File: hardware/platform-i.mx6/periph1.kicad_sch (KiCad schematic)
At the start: 18 parts, among them J1 SD-104031, J3 TC2030-IDC, J6 UART5, J7 I2C4, J8 ECSPI4, U1 IMX6UL_BGA289, U3 TJA1051T, U5 RFM69HCW

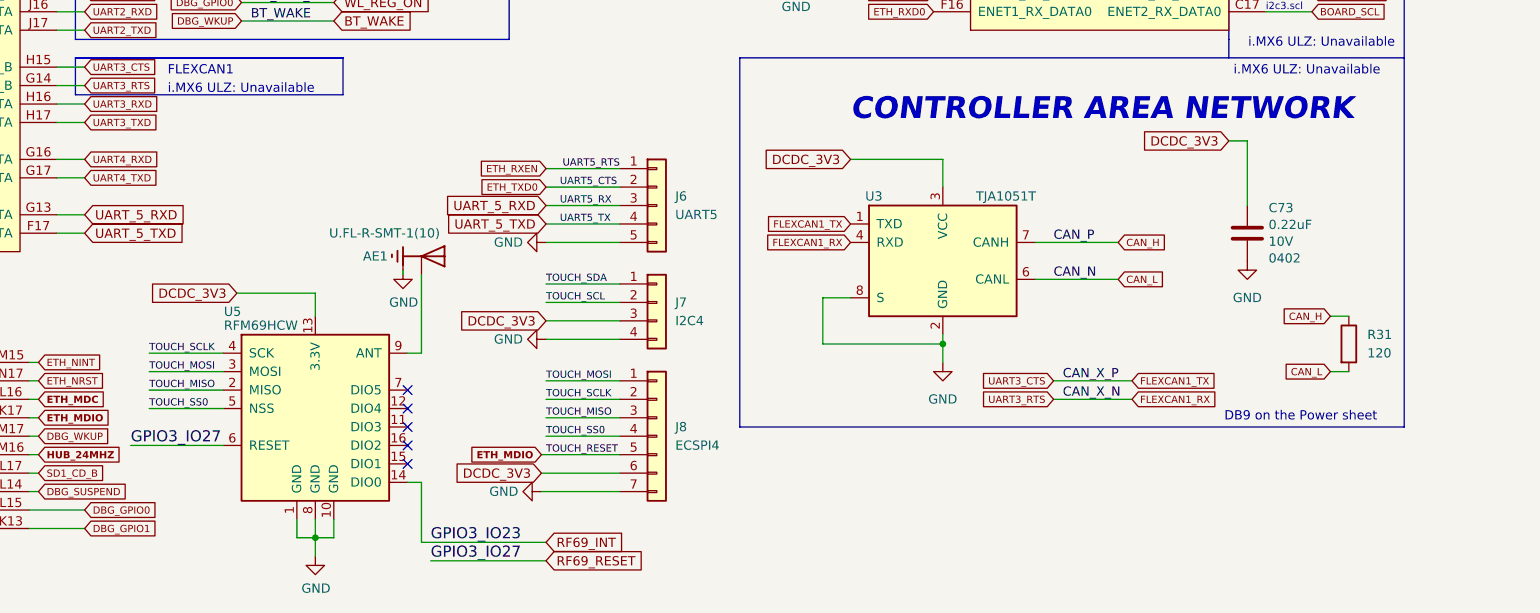
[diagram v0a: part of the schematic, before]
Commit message: Start reworking imx board into the new form factor
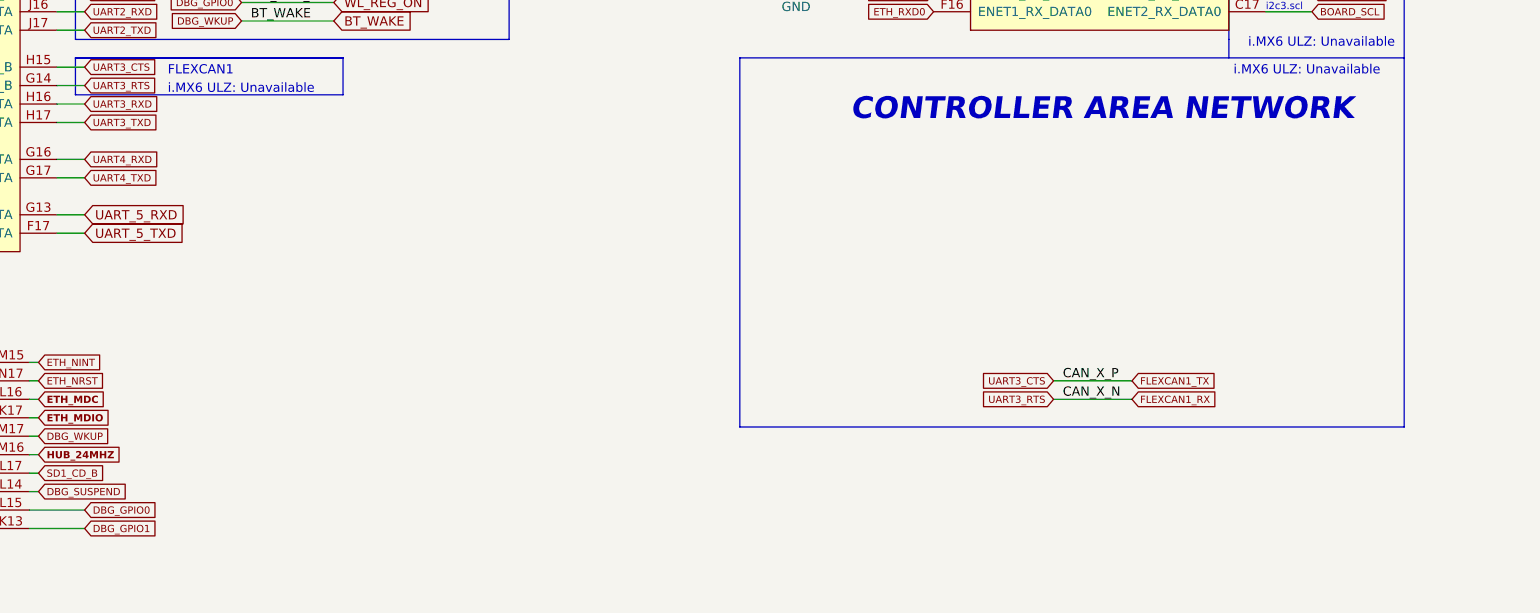
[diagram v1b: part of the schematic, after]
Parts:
- removed AE1: U.FL-R-SMT-1(10), ufl:HRS_U.FL-R-SMT-1(10), symbol U.FL-R-SMT-1_10_:U.FL-R-SMT-1(10)
- removed C73: 0.22uF, Custom Components:C_0402_narrow, symbol Device:C
- removed J6: UART5, Connector_JST:JST_SH_BM05B-SRSS-TB_1x05-1MP_P1.00mm_Vertical, symbol Connector_Generic:Conn_01x05
- removed J7: I2C4, Connector_JST:JST_SH_BM04B-SRSS-TB_1x04-1MP_P1.00mm_Vertical, symbol Connector_Generic:Conn_01x04
- removed J8: ECSPI4, Connector_JST:JST_SH_BM07B-SRSS-TB_1x07-1MP_P1.00mm_Vertical, symbol Connector_Generic:Conn_01x07
- removed R31: 120, Resistor_SMD:R_0805_2012Metric_Pad1.20x1.40mm_HandSolder, symbol Device:R
- removed U3: TJA1051T, Package_SO:SOIC-8_3.9x4.9mm_P1.27mm, symbol Interface_CAN_LIN:TJA1051T
- removed U5: RFM69HCW, rfm69:XCVR_RFM69HW, symbol RF_Module:RFM69HCW
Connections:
- no-connect marks 12 -> 7
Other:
- note removed: "DB9 on the Power sheet"
